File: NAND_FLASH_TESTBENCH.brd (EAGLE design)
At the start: 37.5 x 27.4 mm, 25 parts, among them IC1 S35ML04G300WHI000

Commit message: fixed labels
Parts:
- moved TP10 0.51 mm to (46.2, 41.9)
- moved TP11 0.25 mm to (58.9, 30.0)
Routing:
- net 3.3V: track 40.7 -> 38.8 mm
- net GND: vias 95 -> 89

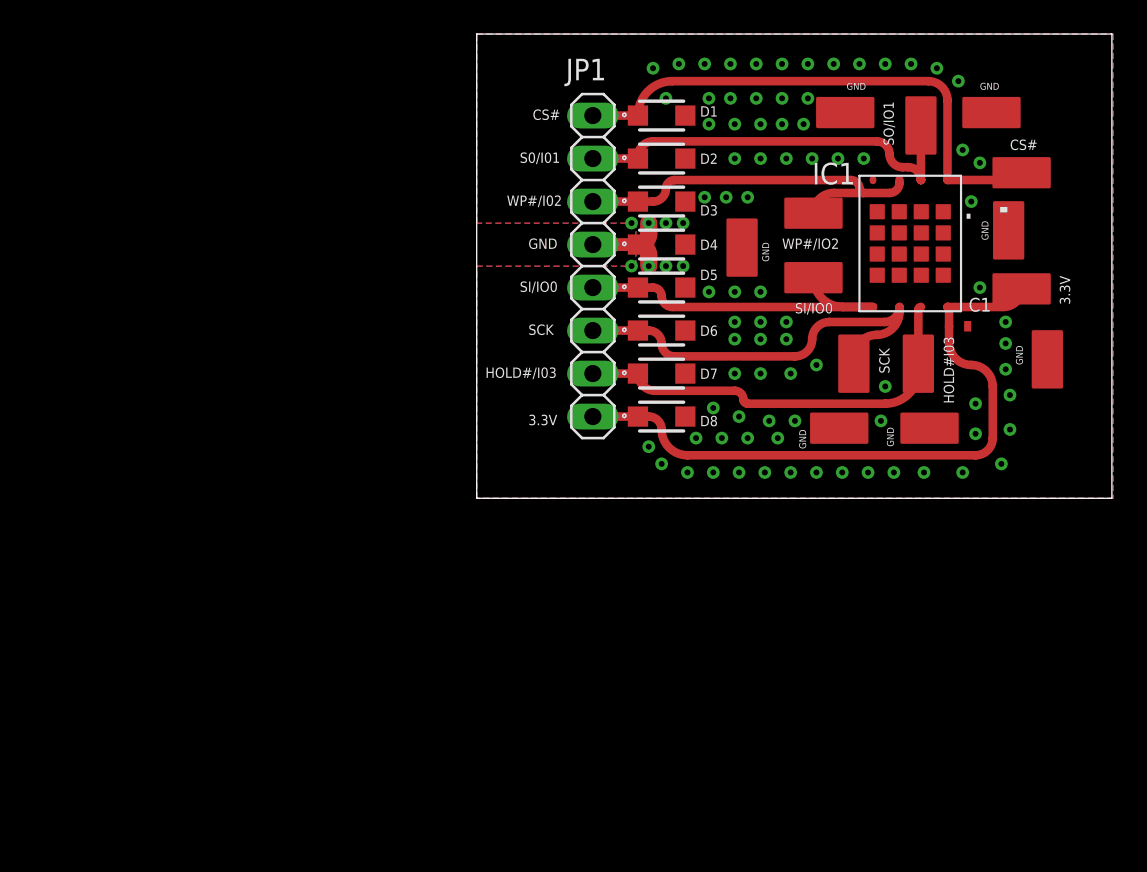
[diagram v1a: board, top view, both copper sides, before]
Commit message: Added Advance circuits logo to PCB and preppared gerberfile for manufacture
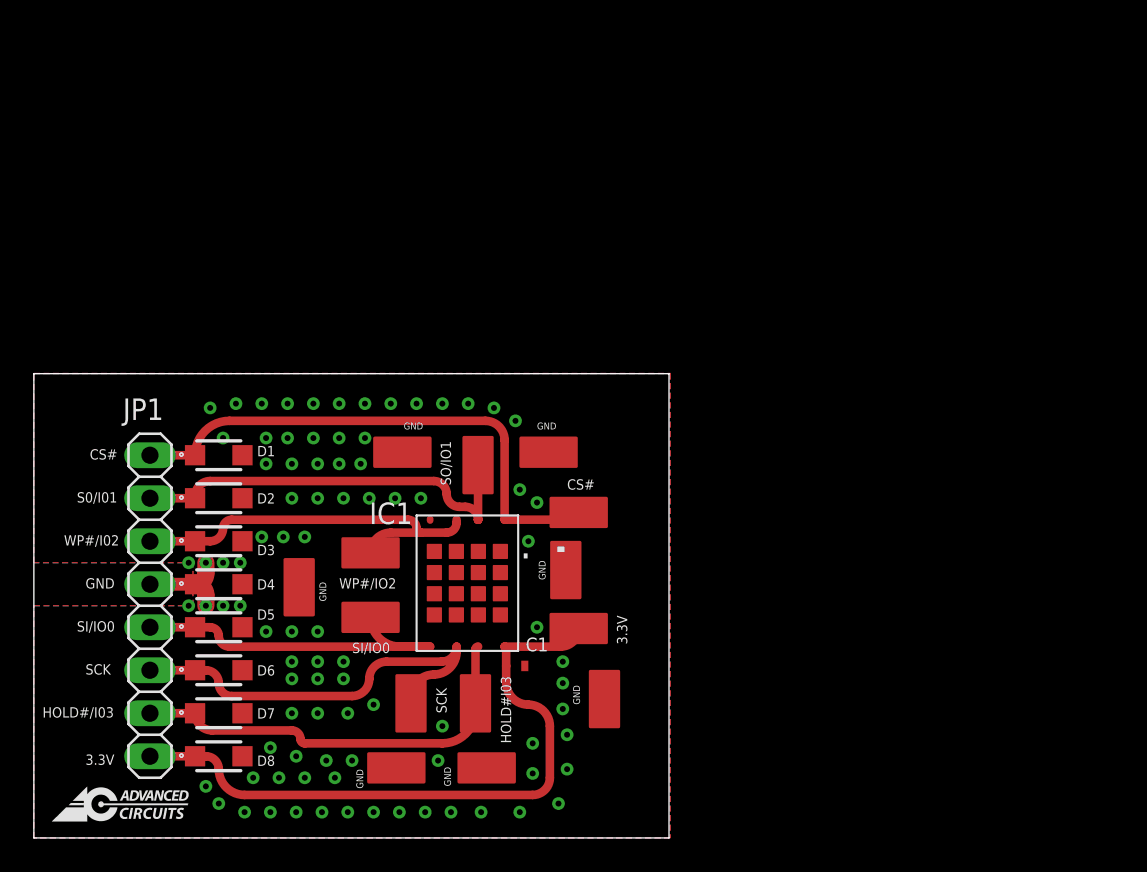
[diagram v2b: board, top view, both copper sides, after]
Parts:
- moved TP2 33.0 mm to (27.2, 20.3)
- moved D1 33.0 mm to (10.9, 22.6)
- moved D2 33.0 mm to (10.9, 20.1)
- moved D3 33.0 mm to (10.9, 17.5)
- moved D4 33.0 mm to (10.9, 15.0)
- moved D5 33.0 mm to (10.9, 12.4)
- moved D6 33.0 mm to (10.9, 9.91)
- moved D7 33.0 mm to (10.9, 7.37)
- moved D8 33.0 mm to (10.9, 4.83)
- moved JP1 33.0 mm to (6.86, 13.7)
- moved TP1 33.0 mm to (30.5, 18.3)
- moved TP11 33.0 mm to (32.8, 9.91)
- moved TP13 33.0 mm to (23.1, 5.08)
- moved TP14 33.0 mm to (14.7, 16.5)
- moved TP3 33.0 mm to (21.6, 17.8)
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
